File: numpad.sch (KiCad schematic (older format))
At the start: 101 parts, among them J1 Conn_02x03_Odd_Even, J3 Battery connectors, SW1 SW_SPST, SW10 SW_SPST, SW11 SW_SPST, SW12 SW_SPST, SW13 SW_SPST, SW14 SW_SPST, SW15 SW_SPST, SW16 SW_SPST, SW17 SW_SPST, SW18 SW_SPST, SW19 SW_SPST, SW2 SW_SPST, SW20 SW_SPST, SW21 SW_SPST, SW22 SW_SPST, SW23 SW_SPST, SW24 SW_SPST, SW27 ON_OFF switch, SW3 SW_SPST, SW4 SW_SPST, SW5 SW_SPST, SW6 SW_SPST, SW7 SW_SPST, SW8 SW_SPST, SW9 SW_SPST, U1 USBLC6-2SC6, U2 MCP73871

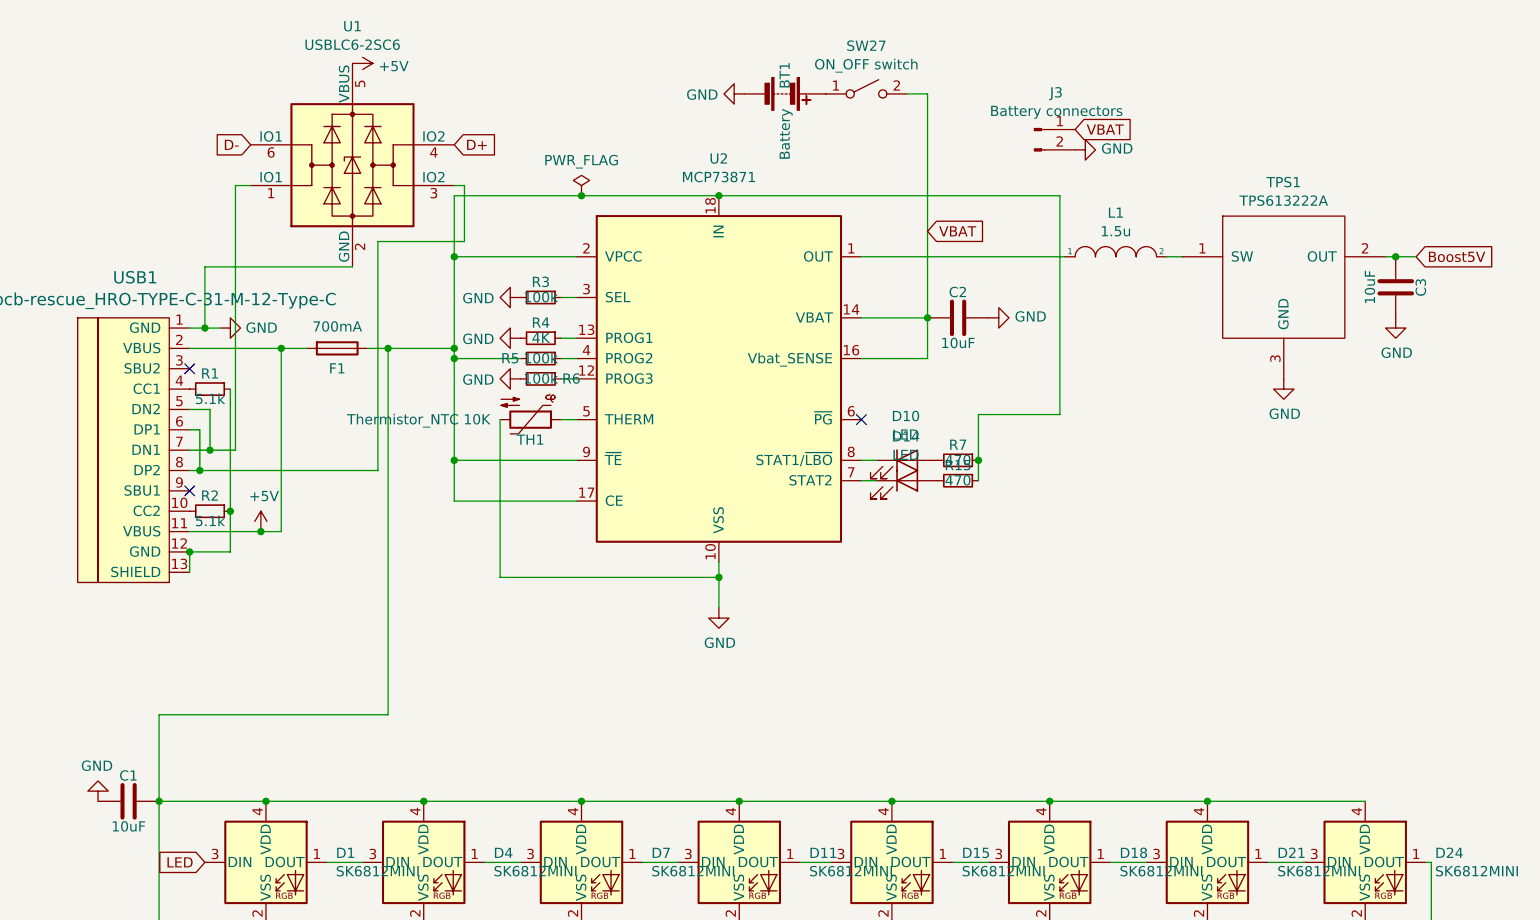
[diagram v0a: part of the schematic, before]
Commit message: Update kicad
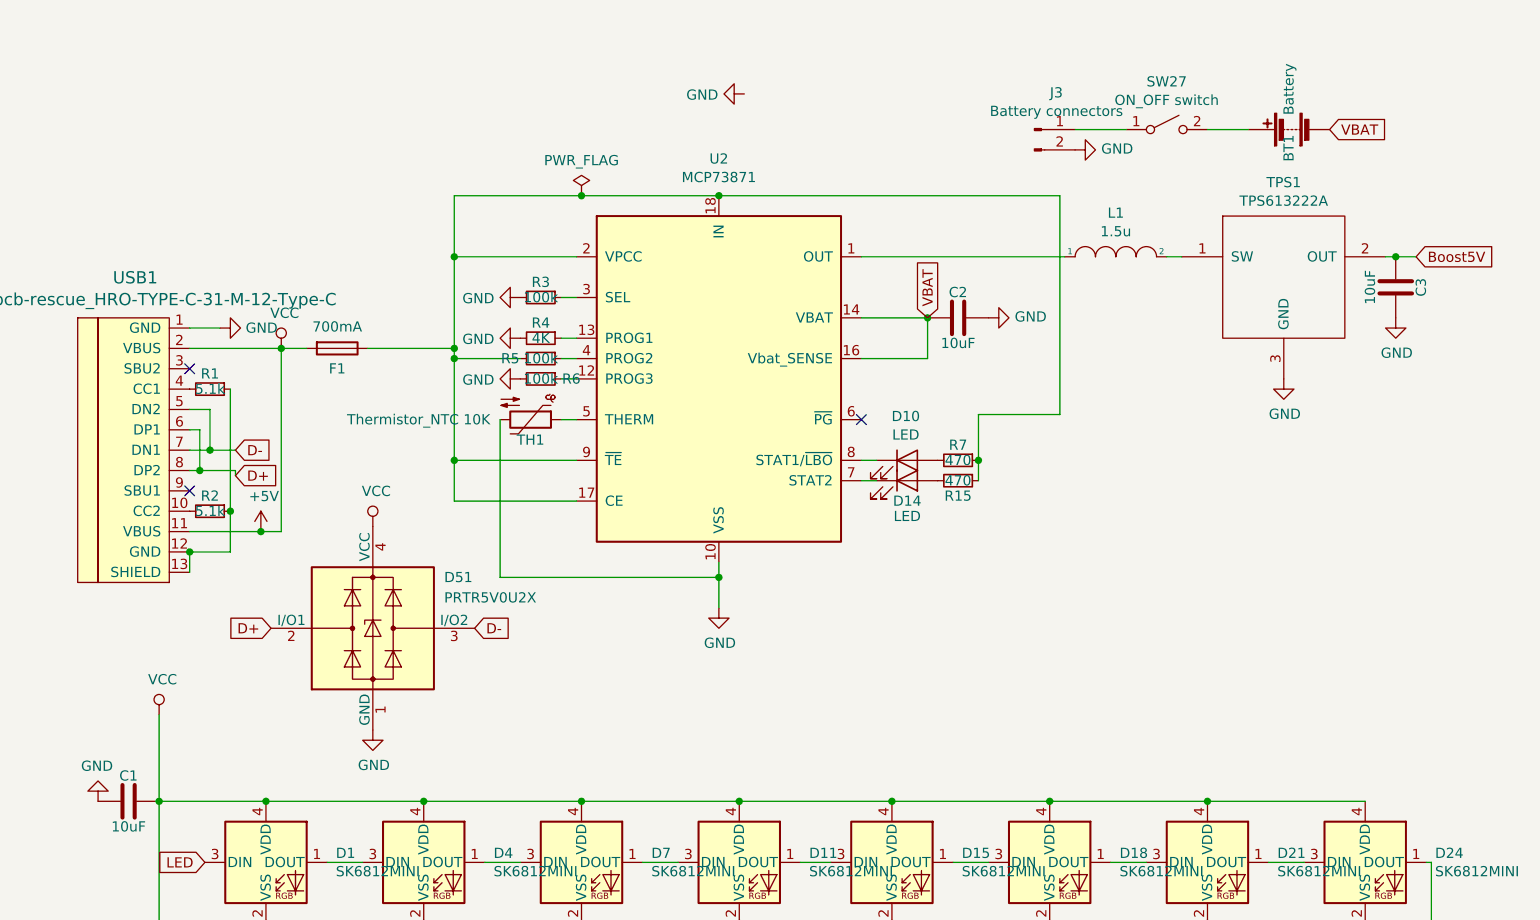
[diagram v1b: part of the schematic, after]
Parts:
- removed U1: USBLC6-2SC6, Package_TO_SOT_SMD:SOT-23-6, symbol Power_Protection:USBLC6-2SC6
- added D51: PRTR5V0U2X, Package_TO_SOT_SMD:SOT-143, symbol Power_Protection:PRTR5V0U2X
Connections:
- net +5V: now also C1.1, D1.4 (VDD), D11.4 (VDD), D12.4 (VDD), D13.4 (VDD), D15.4 (VDD), D16.4 (VDD), D17.4 (VDD), D18.4 (VDD), D19.4 (VDD), D2.4 (VDD), D20.4 (VDD), D21.4 (VDD), D22.4 (VDD), D23.4 (VDD), D24.4 (VDD), D25.4 (VDD), D26.4 (VDD), D3.4 (VDD), D4.4 (VDD), D5.4 (VDD), D6.4 (VDD), D7.4 (VDD), D8.4 (VDD), D9.4 (VDD), D51.4 (VCC)
- net D+: now also USB1.6 (DP1), USB1.8 (DP2), D51.2 (I/O1)
- net D-: now also USB1.5 (DN2), USB1.7 (DN1), D51.3 (I/O2)
- net GND: now also D51.1 (GND); no longer BT1.2 (-)
- net VBAT: now also BT1.2 (-); no longer J3.1 (Pin_1), SW27.2 (B)
- net at BT1.1 (+): now also SW27.2 (B); no longer SW27.1 (A)
- new net: F1.1, R15.1, R5.2, R7.1, U2.17 (CE), U2.18 (IN), U2.19 (IN), U2.2 (VPCC), U2.9 (~TE)
- new net: J3.1 (Pin_1), SW27.1 (A)
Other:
- moved on the sheet: BT1, SW27
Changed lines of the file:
@@
 Comment4 ""
 $EndDescr
-Connection ~ 1050 2500
 Connection ~ 1375 4125
 Connection ~ 1375 4725
@@
 P 1100 2100
 F 0 "R1" V 1025 2100 50  0000 C CNN
-F 1 "5.1k" V 1150 2100 50  0000 C CNN
+F 1 "5.1k" V 1100 2100 50  0000 C CNN
 F 2 "Resistor_SMD:R_0603_1608Metric" H 1100 2100 50  0001 C CNN
 F 3 "~" H 1100 2100 50  0001 C CNN
@@
 P 1100 2700
 F 0 "R2" V 1025 2700 50  0000 C CNN
-F 1 "5.1k" V 1150 2700 50  0000 C CNN
+F 1 "5.1k" V 1100 2700 50  0000 C CNN
 F 2 "Resistor_SMD:R_0603_1608Metric" H 1100 2700 50  0001 C CNN
 F 3 "~" H 1100 2700 50  0001 C CNN
@@
 Wire Wire Line
 	2300 1450 2300 1150
-$Comp
-L Device:Battery BT1
-U 1 1 5E88427C
-P 3925 650
-F 0 "BT1" H 3900 650 50  0000 R CNN
-F 1 "Battery" H 4250 650 50  0000 R CNN
-F 2 "" V 3925 710 50  0001 C CNN
-F 3 "~" V 3925 710 50  0001 C CNN
-	1    3925 650
-	0    1    1    0
-$EndComp
 Wire Wire Line
 	4300 1750 4625 1750
@@
 	0    -1   -1   0
 $EndComp
-Wire Wire Line
-	1000 1800 1075 1800
 $Comp
 L power:GND #PWR07
@@
 U 1 1 5E8DC00E
 P 4525 2550
-F 0 "D14" H 4518 2766 50  0000 C CNN
-F 1 "LED" H 4518 2675 50  0000 C CNN
+F 0 "D14" H 4525 2450 50  0000 C CNN
+F 1 "LED" H 4525 2375 50  0000 C CNN
 F 2 "" H 4525 2550 50  0001 C CNN
 F 3 "~" H 4525 2550 50  0001 C CNN
@@
 U 1 1 5E8EF39A
 P 4775 2550
-F 0 "R15" V 4700 2550 50  0000 C CNN
+F 0 "R15" V 4850 2550 50  0000 C CNN
 F 1 "470" V 4775 2550 50  0000 C CNN
 F 2 "Resistor_SMD:R_0603_1608Metric" H 4775 2550 50  0001 C CNN
@@
 Wire Wire Line
 	1000 1900 1450 1900
-Wire Wire Line
-	1875 1900 1975 1900
 Connection ~ 2300 1900
 Wire Wire Line
@@
 Connection ~ 850  4850
 Wire Wire Line
-	1975 1900 1975 3700
-Wire Wire Line
 	850  3700 850  4125
-Connection ~ 1975 1900
-Wire Wire Line
-	1975 1900 2300 1900
 Connection ~ 850  4125
 $Comp
@@
 	0    1    1    0
 $EndComp
-$Comp
-L Power_Protection:USBLC6-2SC6 U1
-U 1 1 5E9DCADC
-P 1800 1000
-F 0 "U1" H 1800 1681 50  0000 C CNN
-F 1 "USBLC6-2SC6" H 1800 1590 50  0000 C CNN
-F 2 "Package_TO_SOT_SMD:SOT-23-6" H 1050 1400 50  0001 C CNN
-F 3 "http://www2.st.com/resource/en/datasheet/CD00050750.pdf" H 2000 1350 50  0001 C CNN
-	1    1800 1000
-	1    0    0    -1
-$EndComp
-Wire Wire Line
-	1075 1800 1075 1500
-Wire Wire Line
-	1075 1500 1800 1500
-Wire Wire Line
-	850  3700 1975 3700
-Connection ~ 1075 1800
-Wire Wire Line
-	1075 1800 1150 1800
 Wire Wire Line
 	1100 2400 1225 2400
@@
 Wire Wire Line
 	1350 2800 1450 2800
-$Comp
-L power:+5V #PWR03
-U 1 1 5EA1667F
-P 1800 500
-F 0 "#PWR03" H 1800 350 50  0001 C CNN
-F 1 "+5V" V 1815 628 50  0000 L CNN
-F 2 "" H 1800 500 50  0001 C CNN
-F 3 "" H 1800 500 50  0001 C CNN
-	1    1800 500
-	0    1    1    0
-$EndComp
-Text GLabel 1300 900  0    50   Input ~ 0
+Text GLabel 1225 2400 2    50   Input ~ 0
 D-
-Text GLabel 2300 900  2    50   Input ~ 0
+Text GLabel 1225 2525 2    50   Input ~ 0
 D+
-Wire Wire Line
-	1225 2400 1225 1100
-Wire Wire Line
-	1225 1100 1300 1100
-Wire Wire Line
-	1925 2500 1925 1375
-Wire Wire Line
-	1925 1375 2350 1375
-Wire Wire Line
-	2350 1375 2350 1100
-Wire Wire Line
-	2350 1100 2300 1100
-Wire Wire Line
-	1050 2500 1925 2500
 $Comp
 L power:GND #PWR011
@@
 	0    -1   -1   0
 $EndComp
-Text GLabel 5350 825  2    50   Input ~ 0
-VBAT
-Text GLabel 4625 1325 2    50   Input ~ 0
+Text GLabel 4625 1750 1    50   Input ~ 0
 VBAT
 $Comp
 L Switch:SW_SPST SW27
 U 1 1 5EA7EBF1
-P 4325 650
-F 0 "SW27" H 4325 885 50  0000 C CNN
-F 1 "ON_OFF switch" H 4325 794 50  0000 C CNN
-F 2 "" H 4325 650 50  0001 C CNN
-F 3 "~" H 4325 650 50  0001 C CNN
-	1    4325 650
-	1    0    0    -1
-$EndComp
-Wire Wire Line
-	4625 650  4525 650
-Wire Wire Line
-	4625 650  4625 1750
+P 5800 825
+F 0 "SW27" H 5800 1060 50  0000 C CNN
+F 1 "ON_OFF switch" H 5800 969 50  0000 C CNN
+F 2 "" H 5800 825 50  0001 C CNN
+F 3 "~" H 5800 825 50  0001 C CNN
+	1    5800 825
+	1    0    0    -1
+$EndComp
+Wire Wire Line
+	1000 1800 1150 1800
+Wire Wire Line
+	1875 1900 2300 1900
+$Comp
+L power:VCC #PWR015
+U 1 1 5EA8ED18
+P 1450 1900
+F 0 "#PWR015" H 1450 1750 50  0001 C CNN
+F 1 "VCC" H 1467 2073 50  0000 C CNN
+F 2 "" H 1450 1900 50  0001 C CNN
+F 3 "" H 1450 1900 50  0001 C CNN
+	1    1450 1900
+	1    0    0    -1
+$EndComp
+$Comp
+L power:GND #PWR017
+U 1 1 5EA90DB9
+P 1900 3775
+F 0 "#PWR017" H 1900 3525 50  0001 C CNN
+F 1 "GND" H 1905 3602 50  0000 C CNN
+F 2 "" H 1900 3775 50  0001 C CNN
+F 3 "" H 1900 3775 50  0001 C CNN
+	1    1900 3775
+	1    0    0    -1
+$EndComp
+$Comp
+L power:VCC #PWR016
+U 1 1 5EA9128F
+P 1900 2775
+F 0 "#PWR016" H 1900 2625 50  0001 C CNN
+F 1 "VCC" H 1917 2948 50  0000 C CNN
+F 2 "" H 1900 2775 50  0001 C CNN
+F 3 "" H 1900 2775 50  0001 C CNN
+	1    1900 2775
+	1    0    0    -1
+$EndComp
+Text GLabel 1400 3275 0    50   Input ~ 0
+D+
+Wire Wire Line
+	1050 2500 1225 2500
+Wire Wire Line
+	1225 2500 1225 2525
+Connection ~ 1050 2500
+$Comp
+L Device:Battery BT1
+U 1 1 5E88427C
+P 6400 825
+F 0 "BT1" H 6375 825 50  0000 R CNN
+F 1 "Battery" H 6725 825 50  0000 R CNN
+F 2 "" V 6400 885 50  0001 C CNN
+F 3 "~" V 6400 885 50  0001 C CNN
+	1    6400 825
+	0    -1   -1   0
+$EndComp
+Wire Wire Line
+	5350 825  5600 825
+Wire Wire Line
+	6000 825  6200 825
+Text GLabel 6600 825  2    50   Input ~ 0
+VBAT
+$Comp
+L power:VCC #PWR0102
+U 1 1 5EAF14FD
+P 850 3700
+F 0 "#PWR0102" H 850 3550 50  0001 C CNN
+F 1 "VCC" H 867 3873 50  0000 C CNN
+F 2 "" H 850 3700 50  0001 C CNN
+F 3 "" H 850 3700 50  0001 C CNN
+	1    850  3700
+	1    0    0    -1
+$EndComp
+$Comp
+L Power_Protection:PRTR5V0U2X D51
+U 1 1 5EA8FC2A
+P 1900 3275
+F 0 "D51" H 2250 3525 50  0000 L CNN
+F 1 "PRTR5V0U2X" H 2250 3425 50  0000 L CNN
+F 2 "Package_TO_SOT_SMD:SOT-143" H 1960 3275 50  0001 C CNN
+F 3 "https://assets.nexperia.com/documents/data-sheet/PRTR5V0U2X.pdf" H 1960 3275 50  0001 C CNN
+	1    1900 3275
+	1    0    0    -1
+$EndComp
+Text GLabel 2400 3275 2    50   Input ~ 0
+D-
 $EndSCHEMATC

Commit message: Update
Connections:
- net BatGND is gone; now on net GND: C4.2, C5.2, C6.2, C7.2, C8.2, J1.6 (Pin_6)
- net Boost5V is gone; now on net +5V: C3.2, C4.1, C5.1, C6.1, C7.1, C8.1, J1.2 (Pin_2), TPS1.2 (OUT)
- net +5V: no longer C1.1, D1.4 (VDD), D11.4 (VDD), D12.4 (VDD), D13.4 (VDD), D15.4 (VDD), D16.4 (VDD), D17.4 (VDD), D18.4 (VDD), D19.4 (VDD), D2.4 (VDD), D20.4 (VDD), D21.4 (VDD), D22.4 (VDD), D23.4 (VDD), D24.4 (VDD), D25.4 (VDD), D26.4 (VDD), D3.4 (VDD), D4.4 (VDD), D5.4 (VDD), D51.4 (VCC), D6.4 (VDD), D7.4 (VDD), D8.4 (VDD), D9.4 (VDD), F1.2, USB1.11 (VBUS), USB1.2 (VBUS)
- net GND: now also BT1.2 (-), R1.1, R2.1; no longer USB1.1 (GND)
- net VBAT: now also BT1.1 (+), SW27.2 (B); no longer BT1.2 (-)
- net at USB1.12 (GND), USB1.13 (SHIELD): now also USB1.1 (GND); no longer R1.1, R2.1
- new net VCC: C1.1, D1.4 (VDD), D11.4 (VDD), D12.4 (VDD), D13.4 (VDD), D15.4 (VDD), D16.4 (VDD), D17.4 (VDD), D18.4 (VDD), D19.4 (VDD), D2.4 (VDD), D20.4 (VDD), D21.4 (VDD), D22.4 (VDD), D23.4 (VDD), D24.4 (VDD), D25.4 (VDD), D26.4 (VDD), D3.4 (VDD), D4.4 (VDD), D5.4 (VDD), D51.4 (VCC), D6.4 (VDD), D7.4 (VDD), D8.4 (VDD), D9.4 (VDD), F1.2, USB1.11 (VBUS), USB1.2 (VBUS)
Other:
- moved on the sheet: R1, R2
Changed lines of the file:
@@
 $Descr A4 11693 8268
 encoding utf-8
-Sheet 1 2
+Sheet 1 3
 Title ""
 Date ""
@@
 L Device:R_Small R1
 U 1 1 5C8D42DF
-P 1100 2100
-F 0 "R1" V 1025 2100 50  0000 C CNN
-F 1 "5.1k" V 1100 2100 50  0000 C CNN
-F 2 "Resistor_SMD:R_0603_1608Metric" H 1100 2100 50  0001 C CNN
-F 3 "~" H 1100 2100 50  0001 C CNN
-	1    1100 2100
+P 1500 2100
+F 0 "R1" V 1425 2100 50  0000 C CNN
+F 1 "5.1k" V 1575 2100 50  0000 C CNN
+F 2 "Resistor_SMD:R_0603_1608Metric" H 1500 2100 50  0001 C CNN
+F 3 "~" H 1500 2100 50  0001 C CNN
+	1    1500 2100
 	0    1    1    0
 $EndComp
@@
 Text GLabel 9325 6125 2    60   Input ~ 0
 row3
-Text GLabel 9325 6225 2    60   Input ~ 0
-BatGND
-Text GLabel 9325 6025 2    60   Input ~ 0
-Boost5V
-Text GLabel 9100 4700 2    60   Input ~ 0
-Boost5V
-Text GLabel 9100 5275 2    60   Input ~ 0
-BatGND
 Wire Wire Line
 	7075 4425 7100 4425
@@
 Wire Wire Line
 	2300 1150 2925 1150
-Wire Wire Line
-	1200 2700 1200 2900
-Wire Wire Line
-	1200 2100 1200 2700
-Connection ~ 1200 2700
 $Comp
 L Device:R_Small R2
 U 1 1 5E717206
-P 1100 2700
-F 0 "R2" V 1025 2700 50  0000 C CNN
-F 1 "5.1k" V 1100 2700 50  0000 C CNN
-F 2 "Resistor_SMD:R_0603_1608Metric" H 1100 2700 50  0001 C CNN
-F 3 "~" H 1100 2700 50  0001 C CNN
-	1    1100 2700
+P 1500 2700
+F 0 "R2" V 1425 2700 50  0000 C CNN
+F 1 "5.1k" V 1575 2700 50  0000 C CNN
+F 2 "Resistor_SMD:R_0603_1608Metric" H 1500 2700 50  0001 C CNN
+F 3 "~" H 1500 2700 50  0001 C CNN
+	1    1500 2700
 	0    1    1    0
 $EndComp
@@
 Wire Wire Line
 	4300 1750 4625 1750
-$Comp
-L power:GND #PWR08
-U 1 1 5E88DCDE
-P 3725 650
-F 0 "#PWR08" H 3725 400 50  0001 C CNN
-F 1 "GND" V 3730 522 50  0000 R CNN
-F 2 "" H 3725 650 50  0001 C CNN
-F 3 "" H 3725 650 50  0001 C CNN
-	1    3725 650
-	0    1    1    0
-$EndComp
 $Comp
 L Device:C C2
@@
 L power:GND #PWR09
 U 1 1 5E89EF9A
-P 4925 1750
-F 0 "#PWR09" H 4925 1500 50  0001 C CNN
-F 1 "GND" V 4930 1622 50  0000 R CNN
-F 2 "" H 4925 1750 50  0001 C CNN
-F 3 "" H 4925 1750 50  0001 C CNN
-	1    4925 1750
-	0    -1   -1   0
-$EndComp
-$Comp
-L power:GND #PWR01
-U 1 1 5E89F42B
-P 1150 1800
-F 0 "#PWR01" H 1150 1550 50  0001 C CNN
-F 1 "GND" V 1150 1675 50  0000 R CNN
-F 2 "" H 1150 1800 50  0001 C CNN
-F 3 "" H 1150 1800 50  0001 C CNN
-	1    1150 1800
-	0    -1   -1   0
+P 4975 1750
+F 0 "#PWR09" H 4975 1500 50  0001 C CNN
+F 1 "GND" V 4980 1622 50  0000 R CNN
+F 2 "" H 4975 1750 50  0001 C CNN
+F 3 "" H 4975 1750 50  0001 C CNN
+	1    4975 1750
+	1    0    0    -1
 $EndComp
 $Comp
@@
 $EndComp
 Wire Wire Line
-	1000 1900 1450 1900
+	1000 1900 1300 1900
 Connection ~ 2300 1900
 Wire Wire Line
@@
 	1    0    0    -1
 $EndComp
-Text GLabel 7025 1450 2    50   Input ~ 0
-Boost5V
 Wire Wire Line
 	6875 1450 6925 1450
@@
 $EndComp
 Connection ~ 6925 1450
-Wire Wire Line
-	6925 1450 7025 1450
 $Comp
 L pspice:INDUCTOR L1
@@
 	0    1    1    0
 $EndComp
-Wire Wire Line
-	1100 2400 1225 2400
 Connection ~ 1100 2400
-Wire Wire Line
-	1000 2800 1350 2800
-Wire Wire Line
-	1450 2800 1450 1900
-Connection ~ 1450 1900
-Wire Wire Line
-	1450 1900 1575 1900
-$Comp
-L power:+5V #PWR02
-U 1 1 5EA160A9
-P 1350 2800
-F 0 "#PWR02" H 1350 2650 50  0001 C CNN
-F 1 "+5V" H 1365 2973 50  0000 C CNN
-F 2 "" H 1350 2800 50  0001 C CNN
-F 3 "" H 1350 2800 50  0001 C CNN
-	1    1350 2800
-	1    0    0    -1
-$EndComp
-Connection ~ 1350 2800
-Wire Wire Line
-	1350 2800 1450 2800
-Text GLabel 1225 2400 2    50   Input ~ 0
+Text GLabel 1650 2400 2    50   Input ~ 0
 D-
-Text GLabel 1225 2525 2    50   Input ~ 0
+Text GLabel 1650 2500 2    50   Input ~ 0
 D+
 $Comp
@@
 F 3 "" H 550 4125 50  0001 C CNN
 	1    550  4125
-	-1   0    0    1
+	1    0    0    -1
 $EndComp
 $Comp
@@
 L power:GND #PWR014
 U 1 1 5EA7A91F
-P 5350 925
-F 0 "#PWR014" H 5350 675 50  0001 C CNN
-F 1 "GND" V 5355 797 50  0000 R CNN
-F 2 "" H 5350 925 50  0001 C CNN
-F 3 "" H 5350 925 50  0001 C CNN
-	1    5350 925
-	0    -1   -1   0
-$EndComp
-Text GLabel 4625 1750 1    50   Input ~ 0
+P 5425 925
+F 0 "#PWR014" H 5425 675 50  0001 C CNN
+F 1 "GND" V 5430 797 50  0000 R CNN
+F 2 "" H 5425 925 50  0001 C CNN
+F 3 "" H 5425 925 50  0001 C CNN
+	1    5425 925
+	1    0    0    -1
+$EndComp
+Text GLabel 4625 1700 1    50   Input ~ 0
 VBAT
 $Comp
@@
 $EndComp
 Wire Wire Line
-	1000 1800 1150 1800
-Wire Wire Line
 	1875 1900 2300 1900
 $Comp
 L power:VCC #PWR015
 U 1 1 5EA8ED18
-P 1450 1900
-F 0 "#PWR015" H 1450 1750 50  0001 C CNN
-F 1 "VCC" H 1467 2073 50  0000 C CNN
-F 2 "" H 1450 1900 50  0001 C CNN
-F 3 "" H 1450 1900 50  0001 C CNN
-	1    1450 1900
+P 1300 1900
+F 0 "#PWR015" H 1300 1750 50  0001 C CNN
+F 1 "VCC" H 1317 2073 50  0000 C CNN
+F 2 "" H 1300 1900 50  0001 C CNN
+F 3 "" H 1300 1900 50  0001 C CNN
+	1    1300 1900
 	1    0    0    -1
 $EndComp
@@
 Text GLabel 1400 3275 0    50   Input ~ 0
 D+
-Wire Wire Line
-	1050 2500 1225 2500
-Wire Wire Line
-	1225 2500 1225 2525
 Connection ~ 1050 2500
 $Comp
@@
 Wire Wire Line
 	6000 825  6200 825
-Text GLabel 6600 825  2    50   Input ~ 0
+Text GLabel 6100 825  3    50   Input ~ 0
 VBAT
 $Comp
@@
 Text GLabel 2400 3275 2    50   Input ~ 0
 D-
+Wire Wire Line
+	4925 1750 4975 1750
+Wire Wire Line
+	5350 925  5425 925
+Wire Wire Line
+	1000 2800 1300 2800
+Wire Wire Line
+	1000 1800 1200 1800
+Wire Wire Line
+	1100 2400 1650 2400
+Wire Wire Line
+	1050 2500 1650 2500
+Connection ~ 1300 1900
+Wire Wire Line
+	1300 2800 1300 1900
+Wire Wire Line
+	1200 1800 1200 2900
+Wire Wire Line
+	1300 1900 1575 1900
+Wire Wire Line
+	1000 2700 1400 2700
+Wire Wire Line
+	1000 2100 1400 2100
+$Comp
+L power:GND #PWR02
+U 1 1 5E8E9A85
+P 1675 2700
+F 0 "#PWR02" H 1675 2450 50  0001 C CNN
+F 1 "GND" H 1680 2527 50  0000 C CNN
+F 2 "" H 1675 2700 50  0001 C CNN
+F 3 "" H 1675 2700 50  0001 C CNN
+	1    1675 2700
+	1    0    0    -1
+$EndComp
+$Comp
+L power:GND #PWR01
+U 1 1 5E8E9FB5
+P 1675 2100
+F 0 "#PWR01" H 1675 1850 50  0001 C CNN
+F 1 "GND" H 1680 1927 50  0000 C CNN
+F 2 "" H 1675 2100 50  0001 C CNN
+F 3 "" H 1675 2100 50  0001 C CNN
+	1    1675 2100
+	1    0    0    -1
+$EndComp
+Wire Wire Line
+	1600 2100 1675 2100
+Wire Wire Line
+	1600 2700 1675 2700
+Wire Wire Line
+	4625 1750 4625 1700
+$Comp
+L power:GND #PWR03
+U 1 1 5E9132A0
+P 6725 825
+F 0 "#PWR03" H 6725 575 50  0001 C CNN
+F 1 "GND" H 6730 652 50  0000 C CNN
+F 2 "" H 6725 825 50  0001 C CNN
+F 3 "" H 6725 825 50  0001 C CNN
+	1    6725 825
+	1    0    0    -1
+$EndComp
+Wire Wire Line
+	6725 825  6600 825
+$Comp
+L power:+5V #PWR08
+U 1 1 5E9216C0
+P 7225 1450
+F 0 "#PWR08" H 7225 1300 50  0001 C CNN
+F 1 "+5V" H 7240 1623 50  0000 C CNN
+F 2 "" H 7225 1450 50  0001 C CNN
+F 3 "" H 7225 1450 50  0001 C CNN
+	1    7225 1450
+	1    0    0    -1
+$EndComp
+Wire Wire Line
+	6925 1450 7225 1450
+$Comp
+L power:+5V #PWR020
+U 1 1 5E93011A
+P 9675 6025
+F 0 "#PWR020" H 9675 5875 50  0001 C CNN
+F 1 "+5V" H 9690 6198 50  0000 C CNN
+F 2 "" H 9675 6025 50  0001 C CNN
+F 3 "" H 9675 6025 50  0001 C CNN
+	1    9675 6025
+	1    0    0    -1
+$EndComp
+Wire Wire Line
+	9675 6025 9325 6025
+$Comp
+L power:+5V #PWR018
+U 1 1 5E93DC9C
+P 9100 4700
+F 0 "#PWR018" H 9100 4550 50  0001 C CNN
+F 1 "+5V" H 9115 4873 50  0000 C CNN
+F 2 "" H 9100 4700 50  0001 C CNN
+F 3 "" H 9100 4700 50  0001 C CNN
+	1    9100 4700
+	1    0    0    -1
+$EndComp
+$Comp
+L power:GND #PWR021
+U 1 1 5E93E052
+P 9675 6225
+F 0 "#PWR021" H 9675 5975 50  0001 C CNN
+F 1 "GND" H 9680 6052 50  0000 C CNN
+F 2 "" H 9675 6225 50  0001 C CNN
+F 3 "" H 9675 6225 50  0001 C CNN
+	1    9675 6225
+	1    0    0    -1
+$EndComp
+Wire Wire Line
+	9675 6225 9325 6225
+$Comp
+L power:GND #PWR019
+U 1 1 5E94DA92
+P 9100 5275
+F 0 "#PWR019" H 9100 5025 50  0001 C CNN
+F 1 "GND" H 9105 5102 50  0000 C CNN
+F 2 "" H 9100 5275 50  0001 C CNN
+F 3 "" H 9100 5275 50  0001 C CNN
+	1    9100 5275
+	1    0    0    -1
+$EndComp
+$Sheet
+S 13575 4725 2100 1575
+U 5E885BF2
+F0 "Numpad24Keys" 50
+F1 "Numpad24Keys.sch" 50
+$EndSheet
 $EndSCHEMATC
